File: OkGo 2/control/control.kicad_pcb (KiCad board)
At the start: 2 copper layers, 92.2 x 64.5 mm, 69 parts, among them M3_MOUNT VAL**, P102 KEYSW, P105 BATT, P106 ARM_LED, P108 SMA, P110 POWER_SW, P111 SERIAL, P201 CH1, P202 CH2, P205 CH3, P206 CH4, Q201 BSS138BK, Q202 BSS138BK, Q203 BSS138BK, Q204 BSS138BK, U101 SWD, U102 STM32F071CBT6, U103 MEJ2S0305SC, U105 RFM95W, U106 LCD_HD44780, U107 ADP3335, Y101 8MHz

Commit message: Penultimate footprinting, partial #9
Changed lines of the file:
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@@
   )
   (setup
-    (last_trace_width 0.508)
+    (last_trace_width 0.25)
     (user_trace_width 0.254)
     (user_trace_width 0.381)
@@
     (visible_elements FFFFFF1F)
     (pcbplotparams
-      (layerselection 0x01030_00000000)
-      (usegerberextensions false)
-      (excludeedgelayer false)
+      (layerselection 0x01030_80000001)
+      (usegerberextensions true)
+      (excludeedgelayer true)
       (linewidth 0.100000)
       (plotframeref false)
@@
       (psnegative false)
       (psa4output false)
-      (plotreference true)
-      (plotvalue true)
+      (plotreference false)
+      (plotvalue false)
       (plotinvisibletext false)
       (padsonsilk false)
@@
       (drillshape 0)
       (scaleselection 1)
-      (outputdirectory gerbils/))
+      (outputdirectory gerbers))
   )
   (net 0 "")
@@
       (net 16 +5V))
   )
-  (module common:FTSH-105-01-F-D-K (layer F.Cu)
-    (at 175.26 92.837)
-    (fp_text reference U101 (at 2.5 -2.9) (layer F.SilkS) hide
-      (effects (font (size 1 1) (thickness 0.15)))
-    )
-    (fp_text value SWD (at 2.54 3.81) (layer F.SilkS)
-      (effects (font (size 1 1) (thickness 0.15)))
-    )
-    (fp_line (start 5.08 2.3495) (end 5.08 3.175) (layer F.SilkS) (width 0.15))
-    (fp_line (start 5.08 3.175) (end 3.6195 3.175) (layer F.SilkS) (width 0.15))
-    (fp_line (start 3.6195 3.175) (end 3.6195 2.3495) (layer F.SilkS) (width 0.15))
-    (fp_line (start 0 2.3495) (end 0 3.175) (layer F.SilkS) (width 0.15))
-    (fp_line (start 0 3.175) (end 1.4605 3.175) (layer F.SilkS) (width 0.15))
-    (fp_line (start 1.4605 3.175) (end 1.4605 2.3495) (layer F.SilkS) (width 0.15))
-    (fp_line (start 0 -1.0795) (end 0 -1.905) (layer F.SilkS) (width 0.15))
-    (fp_line (start 0 -1.905) (end 5.08 -1.905) (layer F.SilkS) (width 0.15))
-    (fp_line (start 5.08 -1.905) (end 5.08 -1.0795) (layer F.SilkS) (width 0.15))
-    (fp_line (start 2.54 -1.0795) (end 5.715 -1.0795) (layer F.SilkS) (width 0.15))
-    (fp_line (start 5.715 -1.0795) (end 5.715 2.3495) (layer F.SilkS) (width 0.15))
-    (fp_line (start 5.715 2.3495) (end -0.635 2.3495) (layer F.SilkS) (width 0.15))
-    (fp_line (start -0.635 2.3495) (end -0.635 -1.0795) (layer F.SilkS) (width 0.15))
-    (fp_line (start -0.635 -1.0795) (end 2.54 -1.0795) (layer F.SilkS) (width 0.15))
-    (pad 1 thru_hole circle (at 0 1.27) (size 1.016 1.016) (drill 0.635) (layers *.Cu *.Mask F.SilkS)
-      (net 1 +3V3))
-    (pad 2 thru_hole circle (at 0 0) (size 1.016 1.016) (drill 0.635) (layers *.Cu *.Mask F.SilkS)
-      (net 40 /SWDIO))
-    (pad 3 thru_hole circle (at 1.27 1.27) (size 1.016 1.016) (drill 0.635) (layers *.Cu *.Mask F.SilkS)
-      (net 2 GND))
-    (pad 4 thru_hole circle (at 1.27 0) (size 1.016 1.016) (drill 0.635) (layers *.Cu *.Mask F.SilkS)
-      (net 41 /SWDCLK))
-    (pad 5 thru_hole circle (at 2.54 1.27) (size 1.016 1.016) (drill 0.635) (layers *.Cu *.Mask F.SilkS)
-      (net 2 GND))
-    (pad 6 thru_hole circle (at 2.54 0) (size 1.016 1.016) (drill 0.635) (layers *.Cu *.Mask F.SilkS))
-    (pad 7 thru_hole circle (at 3.81 1.27) (size 1.016 1.016) (drill 0.635) (layers *.Cu *.Mask F.SilkS))
-    (pad 8 thru_hole circle (at 3.81 0) (size 1.016 1.016) (drill 0.635) (layers *.Cu *.Mask F.SilkS))
-    (pad 9 thru_hole circle (at 5.08 1.27) (size 1.016 1.016) (drill 0.635) (layers *.Cu *.Mask F.SilkS)
-      (net 2 GND))
-    (pad 10 thru_hole circle (at 5.08 0) (size 1.016 1.016) (drill 0.635) (layers *.Cu *.Mask F.SilkS)
-      (net 3 /nRST))
-  )
   (module common:TESTPOINT (layer F.Cu)
     (at 206.248 120.396)
@@
       (net 2 GND) (zone_connect 1) (thermal_width 0.5) (thermal_gap 0.2))
   )
+  (module common:FTSH-105-01-F-D-K (layer F.Cu)
+    (at 175.26 92.837)
+    (fp_text reference U101 (at 2.5 -2.9) (layer F.SilkS) hide
+      (effects (font (size 1 1) (thickness 0.15)))
+    )
+    (fp_text value SWD (at 2.54 3.81) (layer F.SilkS)
+      (effects (font (size 1 1) (thickness 0.15)))
+    )
+    (fp_line (start 0 3.175) (end 5.08 3.175) (layer F.SilkS) (width 0.15))
+    (fp_line (start 5.08 2.3495) (end 5.08 3.175) (layer F.SilkS) (width 0.15))
+    (fp_line (start 3.6195 3.175) (end 3.6195 2.3495) (layer F.SilkS) (width 0.15))
+    (fp_line (start 0 2.3495) (end 0 3.175) (layer F.SilkS) (width 0.15))
+    (fp_line (start 1.4605 3.175) (end 1.4605 2.3495) (layer F.SilkS) (width 0.15))
+    (fp_line (start 0 -1.0795) (end 0 -1.905) (layer F.SilkS) (width 0.15))
+    (fp_line (start 0 -1.905) (end 5.08 -1.905) (layer F.SilkS) (width 0.15))
+    (fp_line (start 5.08 -1.905) (end 5.08 -1.0795) (layer F.SilkS) (width 0.15))
+    (fp_line (start 2.54 -1.0795) (end 5.715 -1.0795) (layer F.SilkS) (width 0.15))
+    (fp_line (start 5.715 -1.0795) (end 5.715 2.3495) (layer F.SilkS) (width 0.15))
+    (fp_line (start 5.715 2.3495) (end -0.635 2.3495) (layer F.SilkS) (width 0.15))
+    (fp_line (start -0.635 2.3495) (end -0.635 -1.0795) (layer F.SilkS) (width 0.15))
+    (fp_line (start -0.635 -1.0795) (end 2.54 -1.0795) (layer F.SilkS) (width 0.15))
+    (pad 1 thru_hole circle (at 0 1.27) (size 1.016 1.016) (drill 0.635) (layers *.Cu *.Mask F.SilkS)
+      (net 1 +3V3))
+    (pad 2 thru_hole circle (at 0 0) (size 1.016 1.016) (drill 0.635) (layers *.Cu *.Mask F.SilkS)
+      (net 40 /SWDIO))
+    (pad 3 thru_hole circle (at 1.27 1.27) (size 1.016 1.016) (drill 0.635) (layers *.Cu *.Mask F.SilkS)
+      (net 2 GND))
+    (pad 4 thru_hole circle (at 1.27 0) (size 1.016 1.016) (drill 0.635) (layers *.Cu *.Mask F.SilkS)
+      (net 41 /SWDCLK))
+    (pad 5 thru_hole circle (at 2.54 1.27) (size 1.016 1.016) (drill 0.635) (layers *.Cu *.Mask F.SilkS)
+      (net 2 GND))
+    (pad 6 thru_hole circle (at 2.54 0) (size 1.016 1.016) (drill 0.635) (layers *.Cu *.Mask F.SilkS))
+    (pad 7 thru_hole circle (at 3.81 1.27) (size 1.016 1.016) (drill 0.635) (layers *.Cu *.Mask F.SilkS))
+    (pad 8 thru_hole circle (at 3.81 0) (size 1.016 1.016) (drill 0.635) (layers *.Cu *.Mask F.SilkS))
+    (pad 9 thru_hole circle (at 5.08 1.27) (size 1.016 1.016) (drill 0.635) (layers *.Cu *.Mask F.SilkS)
+      (net 2 GND))
+    (pad 10 thru_hole circle (at 5.08 0) (size 1.016 1.016) (drill 0.635) (layers *.Cu *.Mask F.SilkS)
+      (net 3 /nRST))
+  )
   (gr_line (start 145.542 70.866) (end 145.542 71.374) (angle 90) (layer Edge.Cuts) (width 0.1))

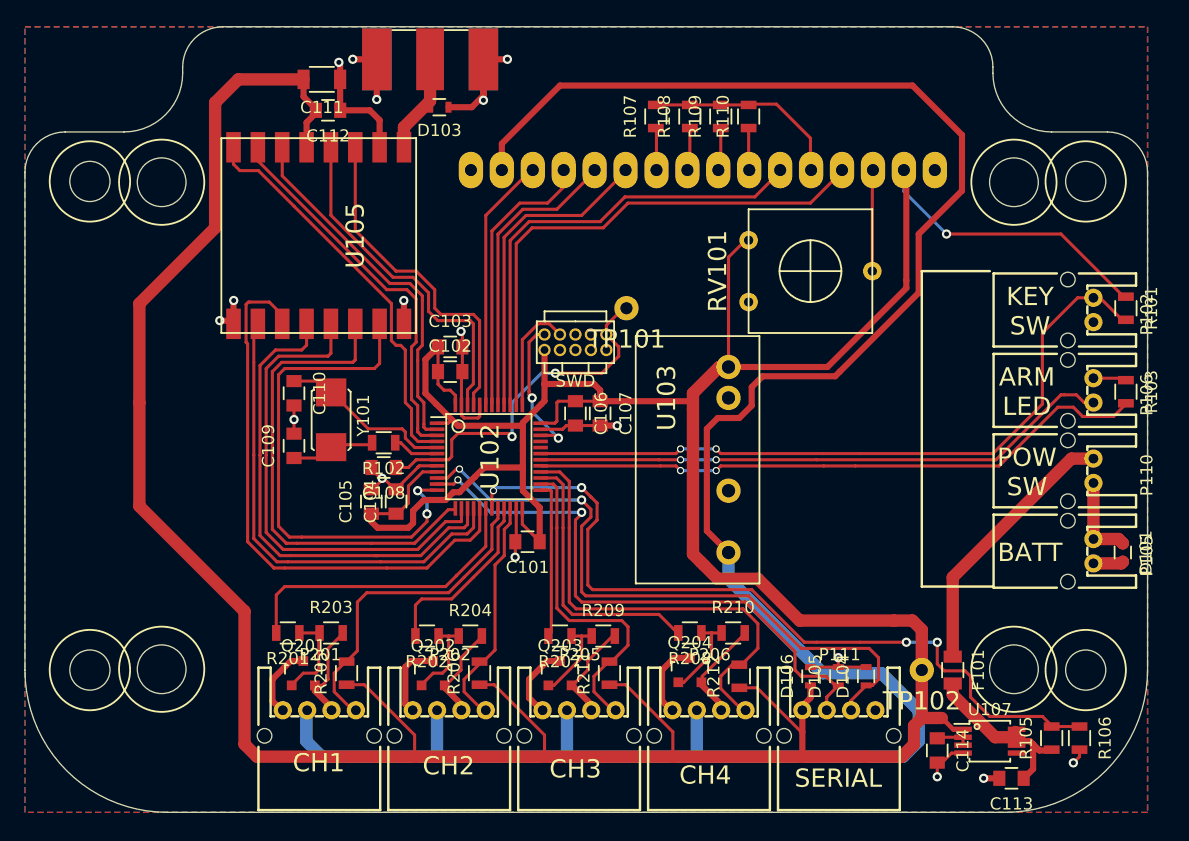
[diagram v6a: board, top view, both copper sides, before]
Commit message: Finished footprinting, resolves #9
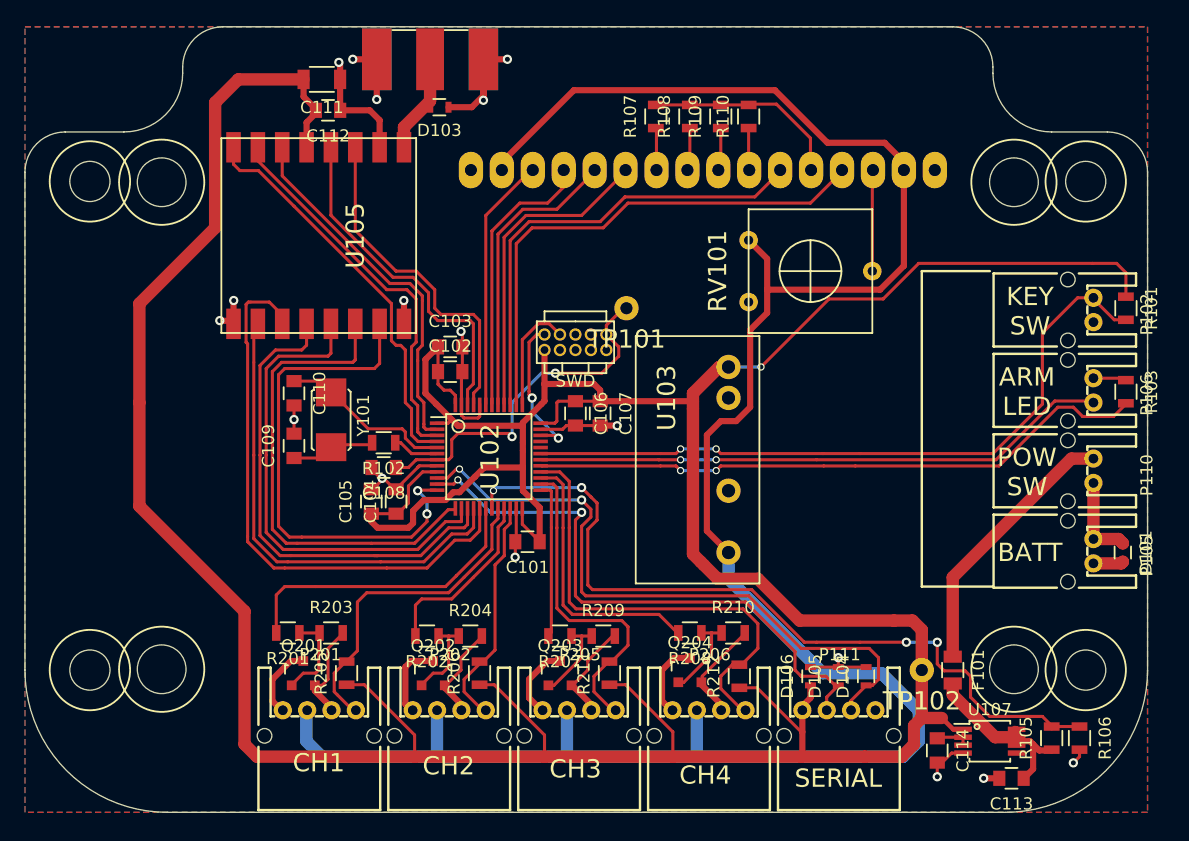
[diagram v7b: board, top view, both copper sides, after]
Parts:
- U106: footprint control:LCD_MC42004A6W -> control:LCD_MC42004A6W_bare
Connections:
- RV101 pad 1: +3V3 -> +5V
- U106 pad 2: +3V3 -> +5V
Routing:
- net +3V3: track 373.9 -> 350.4 mm
- net +5V: track 182.8 -> 179.9 mm

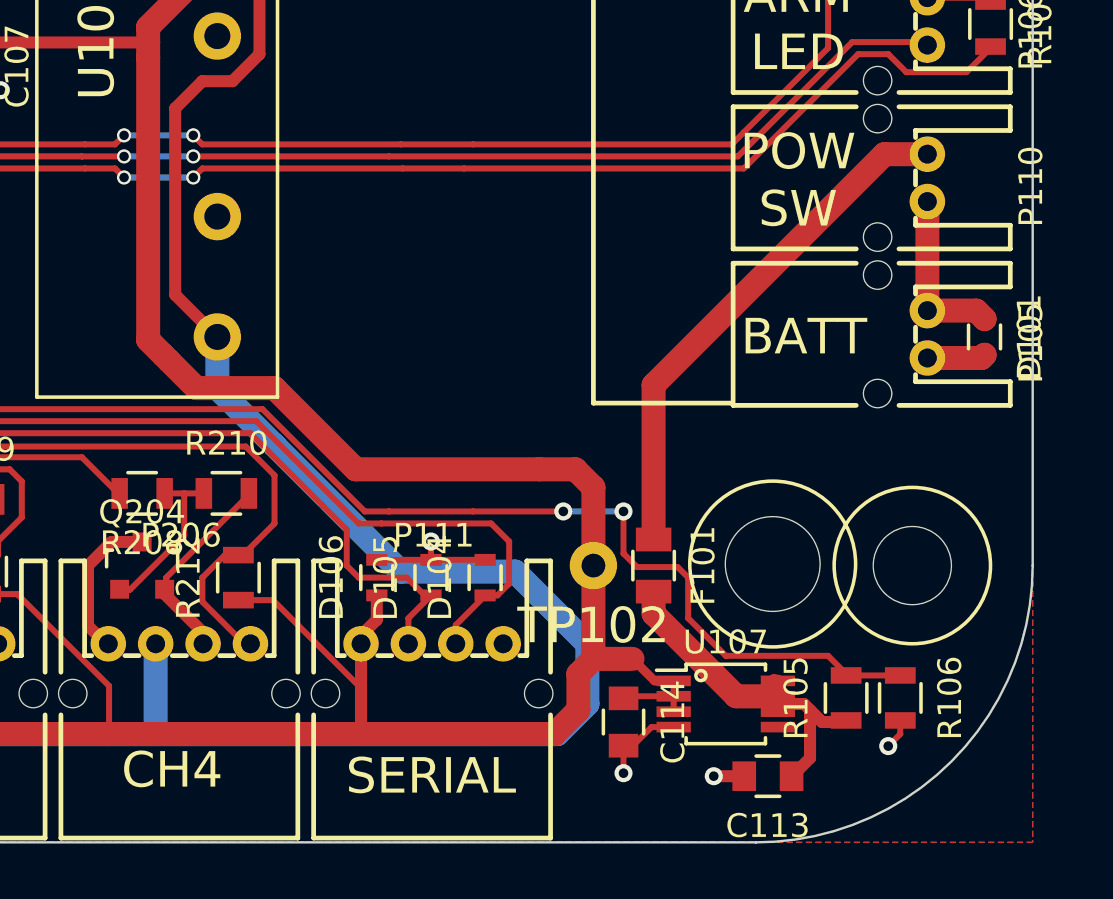
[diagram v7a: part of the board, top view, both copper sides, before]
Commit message: Improved layout of control reg, fixes #41
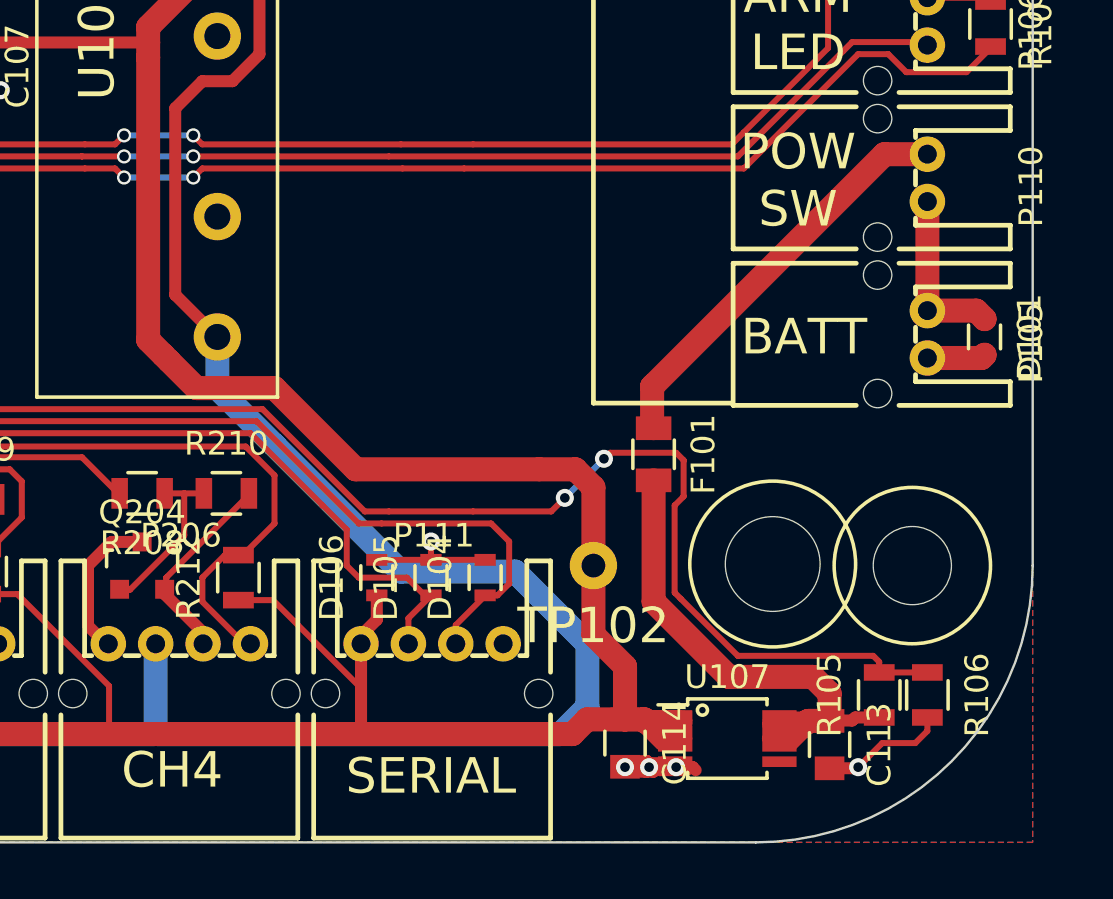
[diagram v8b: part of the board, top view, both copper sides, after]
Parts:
- moved F101 4.70 mm to (208.8, 115.7)
- moved C113 2.93 mm to (216.2, 128.0), turned to 270 degrees
- moved U107 1.46 mm to (211.9, 127.7)
- moved R105 1.40 mm to (218.3, 125.9)
- moved R106 1.15 mm to (220.3, 125.9)
- moved C114 0.89 mm to (207.6, 127.9)
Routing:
- net +BATT: track 16.0 -> 25.3 mm
- net GND: track 130.3 -> 137.8 mm, vias 17 -> 18
- net Net-(F101-Pad1): track 22.6 -> 17.9 mm
- net /BATT_MON: track 66.1 -> 70.5 mm
- net +3V3: track 350.4 -> 352.0 mm
